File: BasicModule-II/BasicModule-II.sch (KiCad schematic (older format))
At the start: 1 part

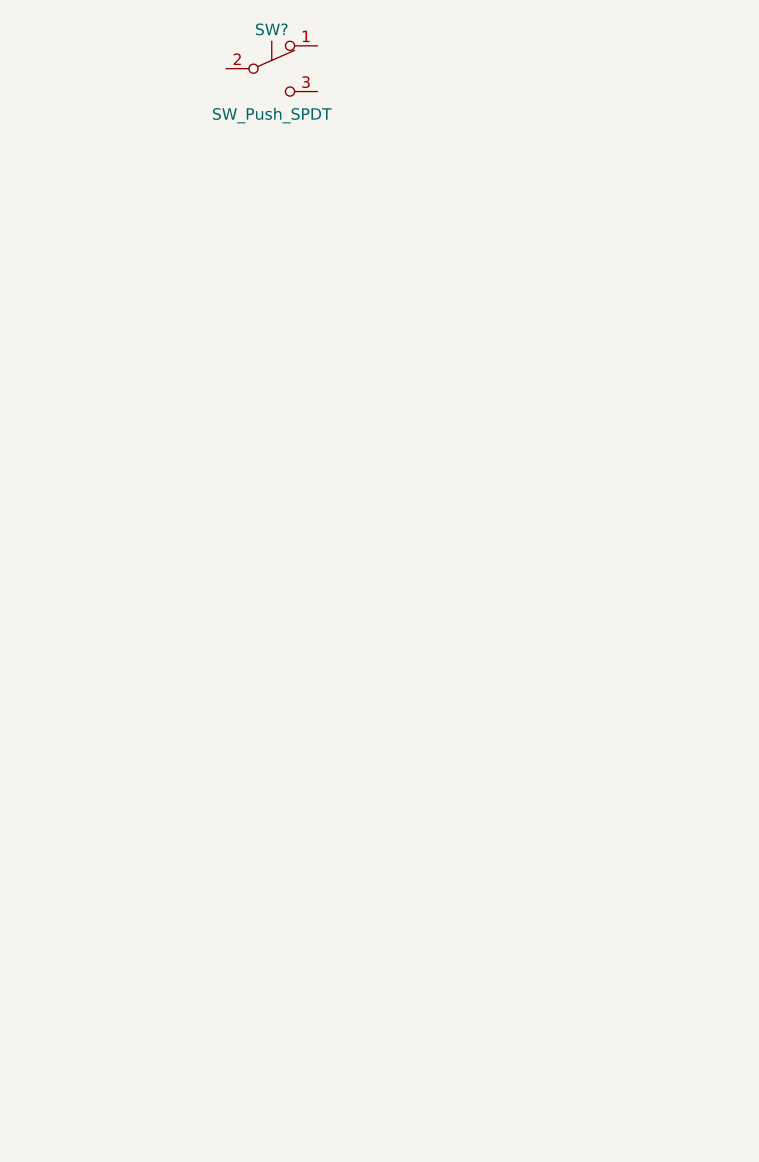
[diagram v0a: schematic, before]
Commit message: ERC pasado, esquema terminado
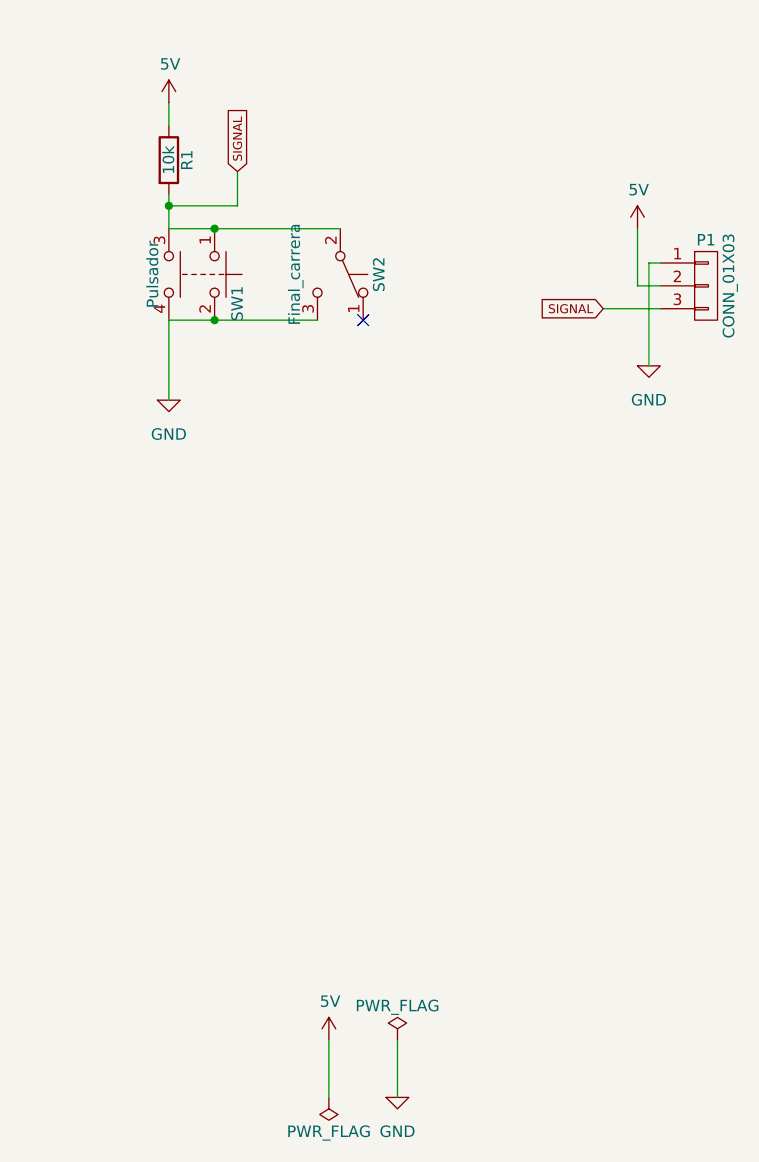
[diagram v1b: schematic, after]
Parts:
- added P1: CONN_01X03, symbol CONN_01X03
- added R1: 10k, symbol R
- added SW1: Pulsador, symbol SW_Push_Dual
- SW2: renamed from SW?; value SW_Push_SPDT -> Final_carrera
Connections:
- net SIGNAL: now reaches SW2.2 (B)
- net SIGNAL: now also P1.3 (P3), R1.2, SW1.1, SW1.3
- net GND: now reaches SW2.3 (C)
- net GND: now also P1.1 (P1), SW1.2, SW1.4
- new net 5V: P1.2 (P2), R1.1
- no-connect marks 0 -> 1
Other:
- moved on the sheet: SW2
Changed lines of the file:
@@
 LIBS:рэс-49
 LIBS:тпг-1
+LIBS:BasicModule-II-cache
 EELAYER 25 0
 EELAYER END
@@
 $EndDescr
 $Comp
-L SW_Push_SPDT SW?
+L SW_Push_SPDT SW2
 U 1 1 5910C1C7
-P 6050 2950
-F 0 "SW?" H 6050 3120 50  0000 C CNN
-F 1 "SW_Push_SPDT" H 6050 2750 50  0000 C CNN
-F 2 "" H 6050 2950 50  0001 C CNN
-F 3 "" H 6050 2950 50  0001 C CNN
-	1    6050 2950
+P 6350 3850
+F 0 "SW2" H 6350 4020 50  0000 C CNN
+F 1 "Final_carrera" H 6350 3650 50  0000 C CNN
+F 2 "" H 6350 3850 50  0001 C CNN
+F 3 "" H 6350 3850 50  0001 C CNN
+	1    6350 3850
+	0    1    1    0
+$EndComp
+$Comp
+L SW_Push_Dual SW1
+U 1 1 59182F02
+P 5800 3850
+F 0 "SW1" H 5850 3950 50  0000 L CNN
+F 1 "Pulsador" H 5800 3580 50  0000 C CNN
+F 2 "" H 5800 4050 50  0001 C CNN
+F 3 "" H 5800 4050 50  0001 C CNN
+	1    5800 3850
+	0    1    1    0
+$EndComp
+$Comp
+L R R1
+U 1 1 59184AE6
+P 5600 3350
+F 0 "R1" V 5680 3350 50  0000 C CNN
+F 1 "10k" V 5600 3350 50  0000 C CNN
+F 2 "" V 5530 3350 50  0001 C CNN
+F 3 "" H 5600 3350 50  0001 C CNN
+	1    5600 3350
 	1    0    0    -1
 $EndComp
+$Comp
+L GND #PWR01
+U 1 1 59184B0B
+P 5600 4400
+F 0 "#PWR01" H 5600 4150 50  0001 C CNN
+F 1 "GND" H 5600 4250 50  0000 C CNN
+F 2 "" H 5600 4400 50  0001 C CNN
+F 3 "" H 5600 4400 50  0001 C CNN
+	1    5600 4400
+	1    0    0    -1
+$EndComp
+$Comp
+L 5V #SUPPLY02
+U 1 1 59184B25
+P 5600 3100
+F 0 "#SUPPLY02" H 5600 3100 50  0001 L BNN
+F 1 "5V" H 5560 3240 50  0000 L BNN
+F 2 "" H 5600 3100 60  0001 C CNN
+F 3 "" H 5600 3100 60  0001 C CNN
+	1    5600 3100
+	1    0    0    -1
+$EndComp
+Wire Wire Line
+	5600 3100 5600 3200
+Wire Wire Line
+	5600 3650 6350 3650
+Wire Wire Line
+	5600 3650 5600 3500
+Wire Wire Line
+	5600 4050 6250 4050
+Wire Wire Line
+	5600 4050 5600 4400
+Connection ~ 5800 3650
+Connection ~ 5800 4050
+NoConn ~ 6450 4050
+Wire Wire Line
+	5600 3550 5900 3550
+Wire Wire Line
+	5900 3550 5900 3400
+Connection ~ 5600 3550
+Text GLabel 5900 3400 1    39   Input ~ 0
+SIGNAL
+$Comp
+L PWR_FLAG #FLG03
+U 1 1 5918535F
+P 6600 7200
+F 0 "#FLG03" H 6600 7275 50  0001 C CNN
+F 1 "PWR_FLAG" H 6600 7350 50  0000 C CNN
+F 2 "" H 6600 7200 50  0001 C CNN
+F 3 "" H 6600 7200 50  0001 C CNN
+	1    6600 7200
+	1    0    0    -1
+$EndComp
+$Comp
+L PWR_FLAG #FLG04
+U 1 1 59185386
+P 6300 7450
+F 0 "#FLG04" H 6300 7525 50  0001 C CNN
+F 1 "PWR_FLAG" H 6300 7600 50  0000 C CNN
+F 2 "" H 6300 7450 50  0001 C CNN
+F 3 "" H 6300 7450 50  0001 C CNN
+	1    6300 7450
+	-1   0    0    1
+$EndComp
+$Comp
+L GND #PWR05
+U 1 1 591853D0
+P 6600 7450
+F 0 "#PWR05" H 6600 7200 50  0001 C CNN
+F 1 "GND" H 6600 7300 50  0000 C CNN
+F 2 "" H 6600 7450 50  0001 C CNN
+F 3 "" H 6600 7450 50  0001 C CNN
+	1    6600 7450
+	1    0    0    -1
+$EndComp
+$Comp
+L 5V #SUPPLY06
+U 1 1 59185438
+P 6300 7200
+F 0 "#SUPPLY06" H 6300 7200 50  0001 L BNN
+F 1 "5V" H 6260 7340 50  0000 L BNN
+F 2 "" H 6300 7200 60  0001 C CNN
+F 3 "" H 6300 7200 60  0001 C CNN
+	1    6300 7200
+	1    0    0    -1
+$EndComp
+Wire Wire Line
+	6300 7200 6300 7450
+Wire Wire Line
+	6600 7450 6600 7200
+$Comp
+L CONN_01X03 P1
+U 1 1 59185582
+P 7950 3900
+F 0 "P1" H 7950 4100 50  0000 C CNN
+F 1 "CONN_01X03" V 8050 3900 50  0000 C CNN
+F 2 "" H 7950 3900 50  0001 C CNN
+F 3 "" H 7950 3900 50  0001 C CNN
+	1    7950 3900
+	1    0    0    -1
+$EndComp
+$Comp
+L GND #PWR07
+U 1 1 5918562D
+P 7700 4250
+F 0 "#PWR07" H 7700 4000 50  0001 C CNN
+F 1 "GND" H 7700 4100 50  0000 C CNN
+F 2 "" H 7700 4250 50  0001 C CNN
+F 3 "" H 7700 4250 50  0001 C CNN
+	1    7700 4250
+	1    0    0    -1
+$EndComp
+$Comp
+L 5V #SUPPLY08
+U 1 1 59185644
+P 7650 3650
+F 0 "#SUPPLY08" H 7650 3650 50  0001 L BNN
+F 1 "5V" H 7610 3790 50  0000 L BNN
+F 2 "" H 7650 3650 60  0001 C CNN
+F 3 "" H 7650 3650 60  0001 C CNN
+	1    7650 3650
+	1    0    0    -1
+$EndComp
+Wire Wire Line
+	7700 4250 7700 3800
+Wire Wire Line
+	7700 3800 7750 3800
+Wire Wire Line
+	7750 3900 7650 3900
+Wire Wire Line
+	7650 3900 7650 3650
+Wire Wire Line
+	7750 4000 7500 4000
+Text GLabel 7500 4000 0    39   Input ~ 0
+SIGNAL
 $EndSCHEMATC

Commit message: LAyout terminado
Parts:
- added R2: R_PHOTO, LEDs:LED-5MM, symbol R_PHOTO
- P1: footprint (none) -> Connectors_JST:JST_PH_S3B-PH-K_03x2.00mm_Angled
- R1: footprint (none) -> Resistors_SMD:R_0805
- SW1: footprint (none) -> Buttons_Switches_THT:SW_PUSH-12mm
- SW2: footprint (none) -> frizzy_switches:limit_sw_tiaihua
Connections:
- net GND: now also R2.2
- net SIGNAL: now also R2.1
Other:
- moved on the sheet: P1
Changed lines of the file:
@@
 F 0 "SW2" H 6350 4020 50  0000 C CNN
 F 1 "Final_carrera" H 6350 3650 50  0000 C CNN
-F 2 "" H 6350 3850 50  0001 C CNN
+F 2 "frizzy_switches:limit_sw_tiaihua" H 6350 3850 50  0001 C CNN
 F 3 "" H 6350 3850 50  0001 C CNN
 	1    6350 3850
@@
 F 0 "SW1" H 5850 3950 50  0000 L CNN
 F 1 "Pulsador" H 5800 3580 50  0000 C CNN
-F 2 "" H 5800 4050 50  0001 C CNN
+F 2 "Buttons_Switches_THT:SW_PUSH-12mm" H 5800 4050 50  0001 C CNN
 F 3 "" H 5800 4050 50  0001 C CNN
 	1    5800 3850
@@
 F 0 "R1" V 5680 3350 50  0000 C CNN
 F 1 "10k" V 5600 3350 50  0000 C CNN
-F 2 "" V 5530 3350 50  0001 C CNN
+F 2 "Resistors_SMD:R_0805" V 5530 3350 50  0001 C CNN
 F 3 "" H 5600 3350 50  0001 C CNN
 	1    5600 3350
@@
 	5600 3100 5600 3200
 Wire Wire Line
-	5600 3650 6350 3650
+	5100 3650 6350 3650
 Wire Wire Line
 	5600 3650 5600 3500
 Wire Wire Line
-	5600 4050 6250 4050
+	5100 4050 6250 4050
 Wire Wire Line
 	5600 4050 5600 4400
@@
 L CONN_01X03 P1
 U 1 1 59185582
-P 7950 3900
-F 0 "P1" H 7950 4100 50  0000 C CNN
-F 1 "CONN_01X03" V 8050 3900 50  0000 C CNN
-F 2 "" H 7950 3900 50  0001 C CNN
-F 3 "" H 7950 3900 50  0001 C CNN
-	1    7950 3900
+P 7400 3900
+F 0 "P1" H 7400 4100 50  0000 C CNN
+F 1 "CONN_01X03" V 7500 3900 50  0000 C CNN
+F 2 "Connectors_JST:JST_PH_S3B-PH-K_03x2.00mm_Angled" H 7400 3900 50  0001 C CNN
+F 3 "" H 7400 3900 50  0001 C CNN
+	1    7400 3900
 	1    0    0    -1
 $EndComp
@@
 L GND #PWR07
 U 1 1 5918562D
-P 7700 4250
-F 0 "#PWR07" H 7700 4000 50  0001 C CNN
-F 1 "GND" H 7700 4100 50  0000 C CNN
-F 2 "" H 7700 4250 50  0001 C CNN
-F 3 "" H 7700 4250 50  0001 C CNN
-	1    7700 4250
+P 7150 4250
+F 0 "#PWR07" H 7150 4000 50  0001 C CNN
+F 1 "GND" H 7150 4100 50  0000 C CNN
+F 2 "" H 7150 4250 50  0001 C CNN
+F 3 "" H 7150 4250 50  0001 C CNN
+	1    7150 4250
 	1    0    0    -1
 $EndComp
@@
 L 5V #SUPPLY08
 U 1 1 59185644
-P 7650 3650
-F 0 "#SUPPLY08" H 7650 3650 50  0001 L BNN
-F 1 "5V" H 7610 3790 50  0000 L BNN
-F 2 "" H 7650 3650 60  0001 C CNN
-F 3 "" H 7650 3650 60  0001 C CNN
-	1    7650 3650
+P 7100 3650
+F 0 "#SUPPLY08" H 7100 3650 50  0001 L BNN
+F 1 "5V" H 7060 3790 50  0000 L BNN
+F 2 "" H 7100 3650 60  0001 C CNN
+F 3 "" H 7100 3650 60  0001 C CNN
+	1    7100 3650
 	1    0    0    -1
 $EndComp
 Wire Wire Line
-	7700 4250 7700 3800
+	7150 4250 7150 3800
 Wire Wire Line
-	7700 3800 7750 3800
+	7150 3800 7200 3800
 Wire Wire Line
-	7750 3900 7650 3900
+	7200 3900 7100 3900
 Wire Wire Line
-	7650 3900 7650 3650
+	7100 3900 7100 3650
 Wire Wire Line
-	7750 4000 7500 4000
-Text GLabel 7500 4000 0    39   Input ~ 0
+	7200 4000 6950 4000
+Text GLabel 6950 4000 0    39   Input ~ 0
 SIGNAL
+$Comp
+L R_PHOTO R2
+U 1 1 59186F6E
+P 5100 3850
+F 0 "R2" H 5150 3900 50  0000 L CNN
+F 1 "R_PHOTO" H 5150 3850 50  0000 L TNN
+F 2 "LEDs:LED-5MM" V 5150 3600 50  0001 L CNN
+F 3 "" H 5100 3800 50  0001 C CNN
+	1    5100 3850
+	1    0    0    -1
+$EndComp
+Wire Wire Line
+	5100 3700 5100 3650
+Connection ~ 5600 3650
+Wire Wire Line
+	5100 4000 5100 4050
+Connection ~ 5600 4050
 $EndSCHEMATC

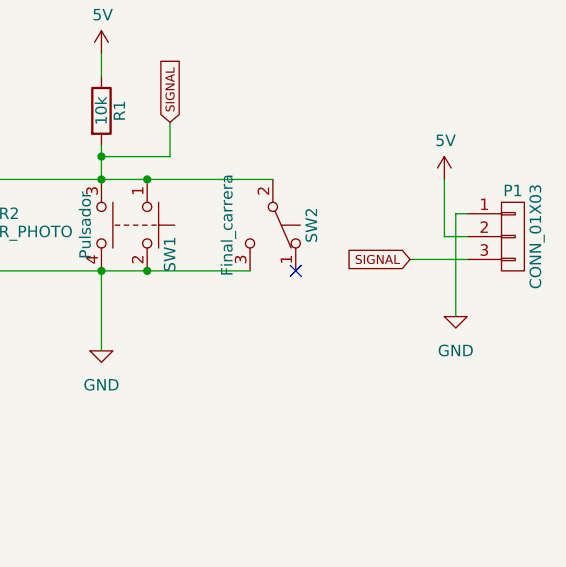
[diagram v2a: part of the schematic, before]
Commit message: Conector cambiado
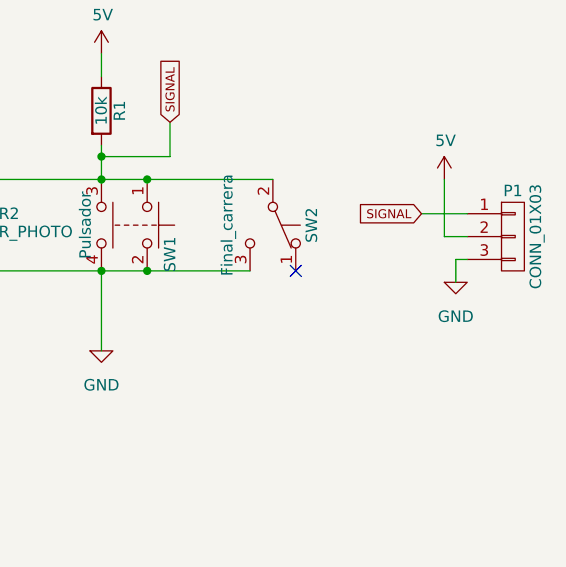
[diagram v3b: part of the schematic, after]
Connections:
- net GND: now also P1.3 (P3); no longer P1.1 (P1)
- net SIGNAL: now also P1.1 (P1); no longer P1.3 (P3)
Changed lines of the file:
@@
 EESchema Schematic File Version 2
-LIBS:power
-LIBS:device
-LIBS:transistors
-LIBS:conn
-LIBS:linear
-LIBS:regul
+LIBS:74xgxx
 LIBS:74xx
-LIBS:cmos4000
-LIBS:adc-dac
-LIBS:memory
-LIBS:xilinx
-LIBS:microcontrollers
-LIBS:dsp
-LIBS:microchip
-LIBS:analog_switches
-LIBS:motorola
-LIBS:texas
-LIBS:intel
-LIBS:audio
-LIBS:interface
-LIBS:digital-audio
-LIBS:philips
-LIBS:display
-LIBS:cypress
-LIBS:siliconi
-LIBS:opto
-LIBS:atmel
-LIBS:contrib
-LIBS:valves
-LIBS:74xgxx
 LIBS:5050_ws2811
 LIBS:a4988-module
@@
 LIBS:actel
 LIBS:adafruit
+LIBS:adc-dac
 LIBS:adxl345
 LIBS:allegro
@@
 LIBS:AMS1117
 LIBS:analog_devices
+LIBS:analog_switches
 LIBS:ant
 LIBS:at24c64
+LIBS:atmel
+LIBS:audio
 LIBS:battery_management
 LIBS:bbd
@@
 LIBS:bosch
 LIBS:brooktre
+LIBS:cmos4000
 LIBS:cmos_ieee
+LIBS:conn
+LIBS:contrib
 LIBS:cp2103
 LIBS:CP2102
+LIBS:cypress
 LIBS:dc-dc
+LIBS:device
 LIBS:dht11
+LIBS:digital-audio
 LIBS:diode
+LIBS:display
+LIBS:dsp
 LIBS:elec-unifil
 LIBS:ESD_Protection
@@
 LIBS:HC164
 LIBS:hlk-rm04
+LIBS:intel
+LIBS:interface
 LIBS:ir
 LIBS:irf7907
@@
 LIBS:Lattice
 LIBS:LilyPad-Wearables
+LIBS:linear
 LIBS:LM2575
 LIBS:logo
@@
 LIBS:MCP3208
 LIBS:mechanical
+LIBS:memory
+LIBS:microchip
 LIBS:microchip_dspic33dsc
 LIBS:microchip_pic10mcu
@@
 LIBS:microchip_pic18mcu
 LIBS:microchip_pic32mcu
+LIBS:microcontrollers
 LIBS:miniusb
 LIBS:motor_drivers
+LIBS:motorola
 LIBS:motors
 LIBS:mp2109dq
@@
 LIBS:OF5032
 LIBS:onsemi
+LIBS:opto
 LIBS:Oscillators
+LIBS:philips
 LIBS:pl2303
 LIBS:pogopin
+LIBS:power
 LIBS:powerint
 LIBS:powerjack
@@
 LIBS:pt4115
 LIBS:references
+LIBS:regul
 LIBS:relays
 LIBS:rfcom
@@
 LIBS:sensors
 LIBS:silabs
+LIBS:siliconi
 LIBS:smd oscillator
 LIBS:songle_relay
@@
 LIBS:Teensy_3_and_LC_Series_Boards_v1.1
 LIBS:test
+LIBS:texas
 LIBS:texas-msp
 LIBS:tp4056
 LIBS:transf
+LIBS:transistors
 LIBS:ts812c
 LIBS:ttl_ieee
@@
 LIBS:usb_ax2
 LIBS:User-Submitted
+LIBS:valves
 LIBS:video
 LIBS:wiznet
@@
 LIBS:XC9572-TQ100
 LIBS:Xicor
+LIBS:xilinx
 LIBS:xilinx_spartan3_virtex4_and_5
 LIBS:zetex
@@
 L GND #PWR07
 U 1 1 5918562D
-P 7150 4250
-F 0 "#PWR07" H 7150 4000 50  0001 C CNN
-F 1 "GND" H 7150 4100 50  0000 C CNN
-F 2 "" H 7150 4250 50  0001 C CNN
-F 3 "" H 7150 4250 50  0001 C CNN
-	1    7150 4250
+P 7150 4100
+F 0 "#PWR07" H 7150 3850 50  0001 C CNN
+F 1 "GND" H 7150 3950 50  0000 C CNN
+F 2 "" H 7150 4100 50  0001 C CNN
+F 3 "" H 7150 4100 50  0001 C CNN
+	1    7150 4100
 	1    0    0    -1
 $EndComp
@@
 $EndComp
 Wire Wire Line
-	7150 4250 7150 3800
-Wire Wire Line
-	7150 3800 7200 3800
+	7000 3800 7200 3800
 Wire Wire Line
 	7200 3900 7100 3900
 Wire Wire Line
 	7100 3900 7100 3650
-Wire Wire Line
-	7200 4000 6950 4000
-Text GLabel 6950 4000 0    39   Input ~ 0
+Text GLabel 7000 3800 0    39   Input ~ 0
 SIGNAL
 $Comp
@@
 	5100 4000 5100 4050
 Connection ~ 5600 4050
+Wire Wire Line
+	7150 4100 7150 4000
+Wire Wire Line
+	7150 4000 7200 4000
 $EndSCHEMATC
